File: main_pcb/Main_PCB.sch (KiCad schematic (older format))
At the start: 52 parts, among them J1 DBG, J2 UI, J3 UI, J4 Raspberry_Pi_Zero_WH, J5 UI, J6 UI, J7 UPDN, J8 ISP, Q1 BSS123, Q2 HSS2307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

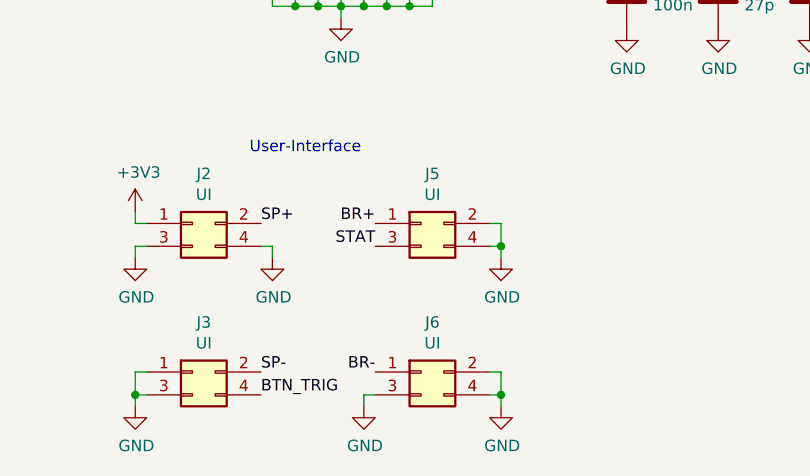
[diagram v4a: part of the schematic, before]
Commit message: Updated main pcb with power button in ui
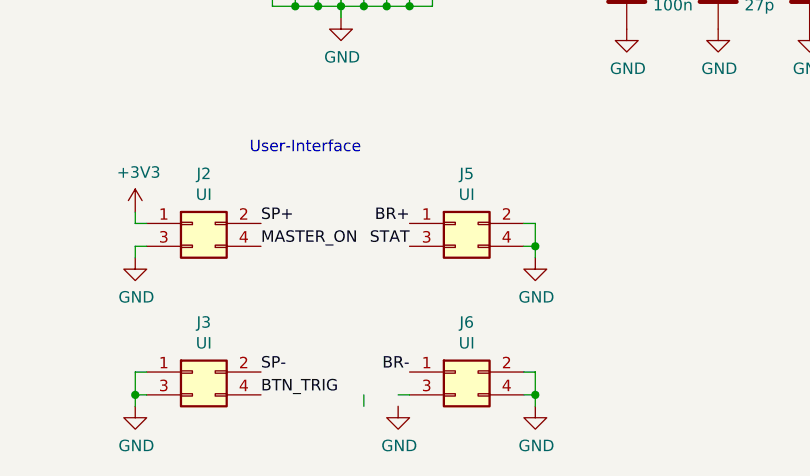
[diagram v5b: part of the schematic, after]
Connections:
- net GND: no longer J2.4 (Pin_4), J6.3 (Pin_3)
- net MASTER_ON: now also J2.4 (Pin_4)
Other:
- moved on the sheet: J5, J6
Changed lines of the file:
@@
 L Connector_Generic:Conn_02x02_Odd_Even J6
 U 1 1 6197FCB5
-P 3800 7250
-F 0 "J6" H 3850 7467 50  0000 C CNN
-F 1 "UI" H 3850 7376 50  0000 C CNN
-F 2 "Connector_PinHeader_2.54mm:PinHeader_2x02_P2.54mm_Vertical" H 3800 7250 50  0001 C CNN
-F 3 "~" H 3800 7250 50  0001 C CNN
-F 4 "C66690" H 3800 7250 50  0001 C CNN "MPN"
-F 5 "BOOMELE" H 3800 7250 50  0001 C CNN "Manufacturer"
-	1    3800 7250
+P 3950 7250
+F 0 "J6" H 4000 7467 50  0000 C CNN
+F 1 "UI" H 4000 7376 50  0000 C CNN
+F 2 "Connector_PinHeader_2.54mm:PinHeader_2x02_P2.54mm_Vertical" H 3950 7250 50  0001 C CNN
+F 3 "~" H 3950 7250 50  0001 C CNN
+F 4 "C66690" H 3950 7250 50  0001 C CNN "MPN"
+F 5 "BOOMELE" H 3950 7250 50  0001 C CNN "Manufacturer"
+	1    3950 7250
 	1    0    0    -1
 $EndComp
@@
 L Connector_Generic:Conn_02x02_Odd_Even J5
 U 1 1 619802E1
-P 3800 6600
-F 0 "J5" H 3850 6817 50  0000 C CNN
-F 1 "UI" H 3850 6726 50  0000 C CNN
-F 2 "Connector_PinHeader_2.54mm:PinHeader_2x02_P2.54mm_Vertical" H 3800 6600 50  0001 C CNN
-F 3 "~" H 3800 6600 50  0001 C CNN
-F 4 "C66690" H 3800 6600 50  0001 C CNN "MPN"
-F 5 "BOOMELE" H 3800 6600 50  0001 C CNN "Manufacturer"
-	1    3800 6600
+P 3950 6600
+F 0 "J5" H 4000 6817 50  0000 C CNN
+F 1 "UI" H 4000 6726 50  0000 C CNN
+F 2 "Connector_PinHeader_2.54mm:PinHeader_2x02_P2.54mm_Vertical" H 3950 6600 50  0001 C CNN
+F 3 "~" H 3950 6600 50  0001 C CNN
+F 4 "C66690" H 3950 6600 50  0001 C CNN "MPN"
+F 5 "BOOMELE" H 3950 6600 50  0001 C CNN "Manufacturer"
+	1    3950 6600
 	1    0    0    -1
 $EndComp
@@
 $EndComp
 $Comp
-L power:GND #PWR010
-U 1 1 61980FC9
-P 3150 6750
-F 0 "#PWR010" H 3150 6500 50  0001 C CNN
-F 1 "GND" H 3155 6577 50  0000 C CNN
-F 2 "" H 3150 6750 50  0001 C CNN
-F 3 "" H 3150 6750 50  0001 C CNN
-	1    3150 6750
-	1    0    0    -1
-$EndComp
-$Comp
 L power:GND #PWR013
 U 1 1 61981281
-P 3550 7400
-F 0 "#PWR013" H 3550 7150 50  0001 C CNN
-F 1 "GND" H 3555 7227 50  0000 C CNN
-F 2 "" H 3550 7400 50  0001 C CNN
-F 3 "" H 3550 7400 50  0001 C CNN
-	1    3550 7400
+P 3700 7400
+F 0 "#PWR013" H 3700 7150 50  0001 C CNN
+F 1 "GND" H 3705 7227 50  0000 C CNN
+F 2 "" H 3700 7400 50  0001 C CNN
+F 3 "" H 3700 7400 50  0001 C CNN
+	1    3700 7400
 	1    0    0    -1
 $EndComp
@@
 L power:GND #PWR016
 U 1 1 61981744
-P 4150 7400
-F 0 "#PWR016" H 4150 7150 50  0001 C CNN
-F 1 "GND" H 4155 7227 50  0000 C CNN
-F 2 "" H 4150 7400 50  0001 C CNN
-F 3 "" H 4150 7400 50  0001 C CNN
-	1    4150 7400
+P 4300 7400
+F 0 "#PWR016" H 4300 7150 50  0001 C CNN
+F 1 "GND" H 4305 7227 50  0000 C CNN
+F 2 "" H 4300 7400 50  0001 C CNN
+F 3 "" H 4300 7400 50  0001 C CNN
+	1    4300 7400
 	1    0    0    -1
 $EndComp
@@
 L power:GND #PWR015
 U 1 1 61981CE1
-P 4150 6750
-F 0 "#PWR015" H 4150 6500 50  0001 C CNN
-F 1 "GND" H 4155 6577 50  0000 C CNN
-F 2 "" H 4150 6750 50  0001 C CNN
-F 3 "" H 4150 6750 50  0001 C CNN
-	1    4150 6750
-	1    0    0    -1
-$EndComp
-Wire Wire Line
-	4100 6600 4150 6600
-Wire Wire Line
-	4150 6600 4150 6700
-Wire Wire Line
-	4100 6700 4150 6700
-Connection ~ 4150 6700
-Wire Wire Line
-	4150 6700 4150 6750
-Wire Wire Line
-	4100 7250 4150 7250
-Wire Wire Line
-	4150 7250 4150 7350
-Wire Wire Line
-	4100 7350 4150 7350
-Connection ~ 4150 7350
-Wire Wire Line
-	4150 7350 4150 7400
-Wire Wire Line
-	3600 7350 3550 7350
+P 4300 6750
+F 0 "#PWR015" H 4300 6500 50  0001 C CNN
+F 1 "GND" H 4305 6577 50  0000 C CNN
+F 2 "" H 4300 6750 50  0001 C CNN
+F 3 "" H 4300 6750 50  0001 C CNN
+	1    4300 6750
+	1    0    0    -1
+$EndComp
+Wire Wire Line
+	4250 6600 4300 6600
+Wire Wire Line
+	4300 6600 4300 6700
+Wire Wire Line
+	4250 6700 4300 6700
+Connection ~ 4300 6700
+Wire Wire Line
+	4300 6700 4300 6750
+Wire Wire Line
+	4250 7250 4300 7250
+Wire Wire Line
+	4300 7250 4300 7350
+Wire Wire Line
+	4250 7350 4300 7350
+Connection ~ 4300 7350
+Wire Wire Line
+	4300 7350 4300 7400
+Wire Wire Line
+	3750 7350 3700 7350
 Wire Wire Line
 	3550 7350 3550 7400
@@
 Text Label 3100 7250 0    50   ~ 0
 SP-
-Text Label 3600 6600 2    50   ~ 0
+Text Label 3750 6600 2    50   ~ 0
 BR+
-Text Label 3600 7250 2    50   ~ 0
+Text Label 3750 7250 2    50   ~ 0
 BR-
-Text Label 3600 6700 2    50   ~ 0
+Text Label 3750 6700 2    50   ~ 0
 STAT
 Text Notes 3050 6300 0    50   ~ 0
@@
 Wire Wire Line
 	2550 6600 2550 6550
-Wire Wire Line
-	3100 6700 3150 6700
-Wire Wire Line
-	3150 6700 3150 6750
 Text Label 9650 4600 0    50   ~ 0
 UC_TX
@@
 NoConn ~ 4350 4200
 NoConn ~ 2750 4900
+Text Label 3100 6700 0    50   ~ 0
+MASTER_ON
 $EndSCHEMATC
